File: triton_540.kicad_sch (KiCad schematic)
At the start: 46 parts, among them J1 REC ANT, J3 Conn_01x04, J4 AUX 12V, J5 KEY, J6 PTT, Q2 MPS6514, Y1 13.99MHz, Y2 14.49MHz, Y3 14.99MHz, Y4 15.49MHz

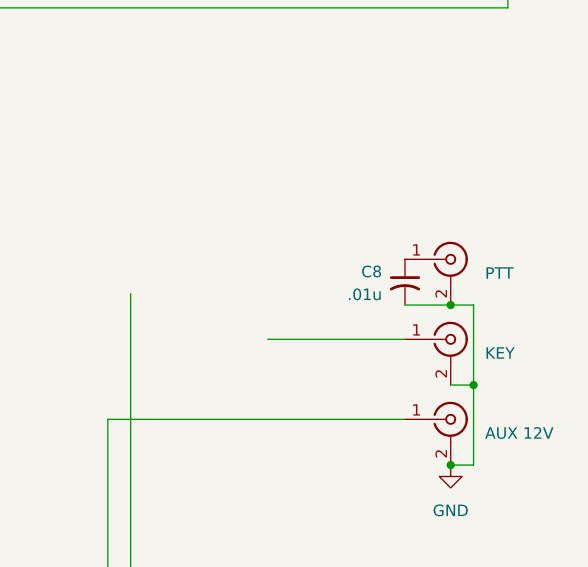
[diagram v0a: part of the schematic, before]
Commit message: Rename sub-sheets by assembly number and clear the duplicate designator
Give the four sub-sheets one filename convention, assembly number first, so
each board's schematic sorts beside its document:

  RF_Amp_80166      -> 80166_rf_amp
  if-agc_80279      -> 80279_if_agc
  tx_rx_mixer_80287 -> 80287_tx_rx_mixer
  VFO_80289         -> 80289_vfo

Update the four Sheetfile properties in triton_540.kicad_sch, the six 80279
runners that open their sheet by name, the preflight script, and thirteen
documentation references.

Sheetname is deliberately untouched. KiCad derives SPICE net prefixes from it,
so /rf_amp_80166/ and its siblings are hard-coded in the study runners and
baked into every retained study CSV; renaming a sheet would invalidate that
evidence. Filenames and sheet names therefore diverge, and the sheet names keep
their inconsistent styles.

Two different capacitors both carried the reference C8: the 10 pF in the 80166
L1 band-capacitor run, and a 0.01 uF bypass by the rear-apron PTT, KEY and AUX
jacks. The 10 pF is the documented C8; the bypass is now C2, which clears the
annotation error that kicad-cli reported on every netlist export.

Netlist export before and after the renames is byte-identical, confirming all
four sheets still resolve and no net name moved. Both sheets that tooling opens
standalone export cleanly on their own.

Record the layout, sheet-name and tooling conventions in AGENTS.md, including
that a duplicate designator is resolved from the manual rather than by taking
the next free number.

Co-Authored-By: Claude Opus 5 <noreply@anthropic.com>
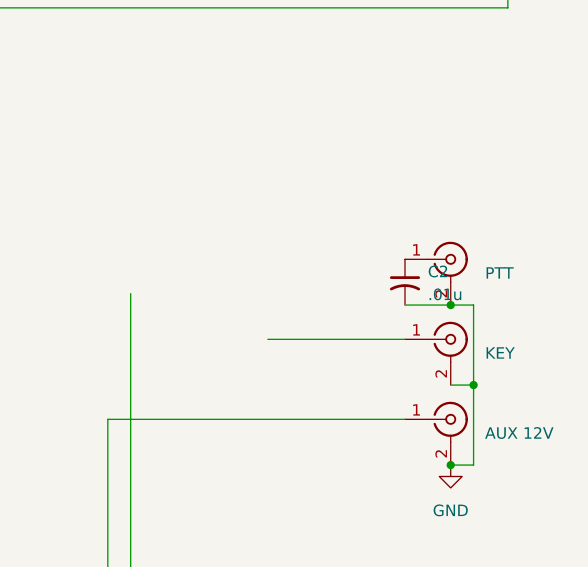
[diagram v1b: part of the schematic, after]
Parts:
- renumbered C8 to C2
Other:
- sheet IF-AGC_80279: file if-agc_80279.kicad_sch -> 80279_if_agc.kicad_sch
- sheet RF_Amp_80166: file RF_Amp_80166.kicad_sch -> 80166_rf_amp.kicad_sch
- sheet TX RX Mixer 80287: file tx_rx_mixer_80287.kicad_sch -> 80287_tx_rx_mixer.kicad_sch
- sheet VFO-80289: file VFO_80289.kicad_sch -> 80289_vfo.kicad_sch
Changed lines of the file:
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@@
 		(dnp no)
 		(fields_autoplaced yes)
-		(property "Reference" "C8"
-			(at 397.51 139.8269 0)
-			(show_name no)
-			(do_not_autoplace no)
-			(effects
-				(font
-					(size 1.27 1.27)
-				)
-				(justify right)
+		(property "Reference" "C2"
+			(at 402.59 139.8269 0)
+			(show_name no)
+			(do_not_autoplace no)
+			(effects
+				(font
+					(size 1.27 1.27)
+				)
+				(justify left)
 			)
 		)
 		(property "Value" ".01u"
-			(at 397.51 142.3669 0)
-			(show_name no)
-			(do_not_autoplace no)
-			(effects
-				(font
-					(size 1.27 1.27)
-				)
-				(justify right)
+			(at 402.59 142.3669 0)
+			(show_name no)
+			(do_not_autoplace no)
+			(effects
+				(font
+					(size 1.27 1.27)
+				)
+				(justify left)
 			)
 		)
@@
 			(project "triton_540"
 				(path "/2d45daab-5f60-4e97-8c02-32b0054eab28"
-					(reference "C8")
+					(reference "C2")
 					(unit 1)
 				)
@@
 			)
 		)
-		(property "Sheetfile" "if-agc_80279.kicad_sch"
+		(property "Sheetfile" "80279_if_agc.kicad_sch"
 			(at 236.22 47.5746 0)
 			(hide yes)
@@
 			)
 		)
-		(property "Sheetfile" "RF_Amp_80166.kicad_sch"
+		(property "Sheetfile" "80166_rf_amp.kicad_sch"
 			(at 38.1 38.6846 0)
 			(hide yes)
@@
 			)
 		)
-		(property "Sheetfile" "VFO_80289.kicad_sch"
+		(property "Sheetfile" "80289_vfo.kicad_sch"
 			(at 186.69 128.8546 0)
 			(hide yes)
@@
 			)
 		)
-		(property "Sheetfile" "tx_rx_mixer_80287.kicad_sch"
+		(property "Sheetfile" "80287_tx_rx_mixer.kicad_sch"
 			(at 167.64 47.5746 0)
 			(hide yes)
